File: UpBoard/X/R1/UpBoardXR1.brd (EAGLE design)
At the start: 88.9 x 76.2 mm, 79 parts, among them CN1 100nF, CN2 100nF, CN3 100nF, CN4 100nF, IC1 SAM3X8E(ARDUINO), IC2 W25N01GVZEIG/IT, Q2 MBT3904DW2T1, X1 16POS_RIBBON, X2 16POS_RIBBON, X3 16POS_RIBBON, X4 16POS_RIBBON, Y1 FH1200001, Y2 ABS05

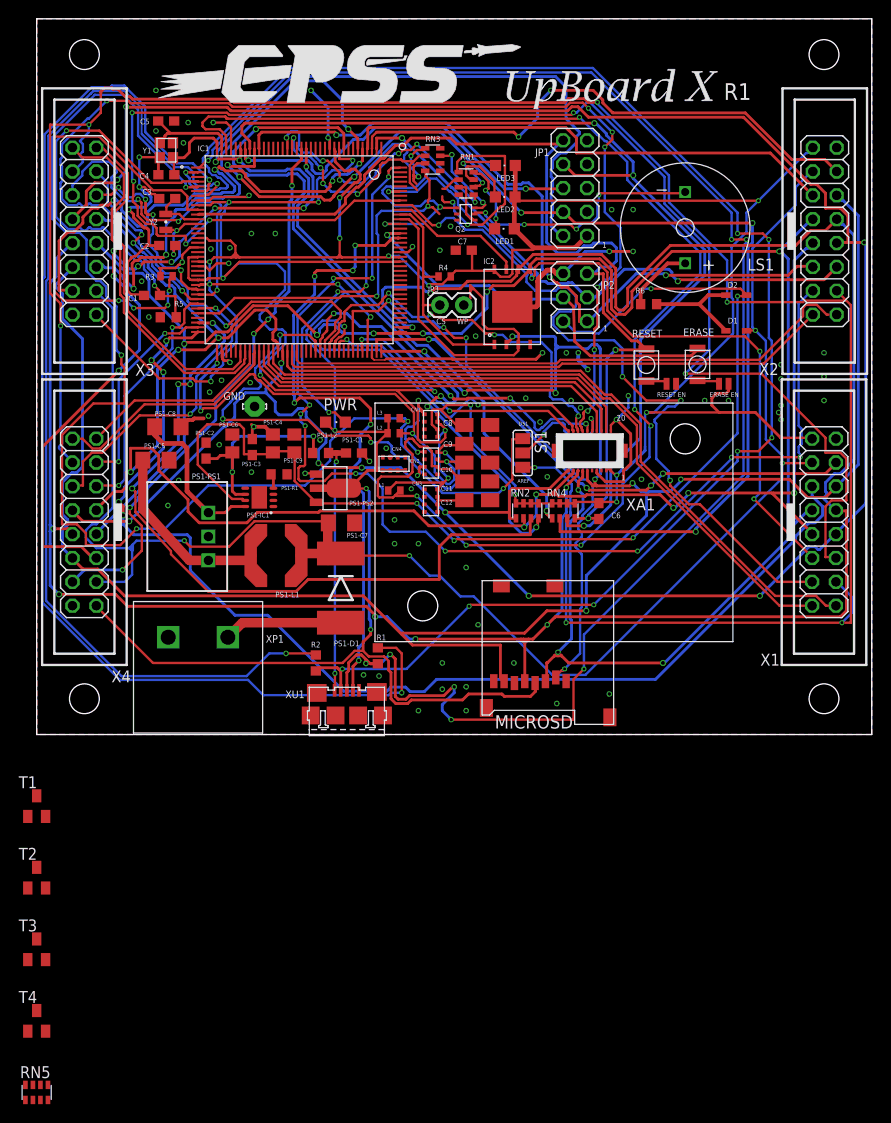
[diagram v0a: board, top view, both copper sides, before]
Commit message: Added in and routed bjt arrays
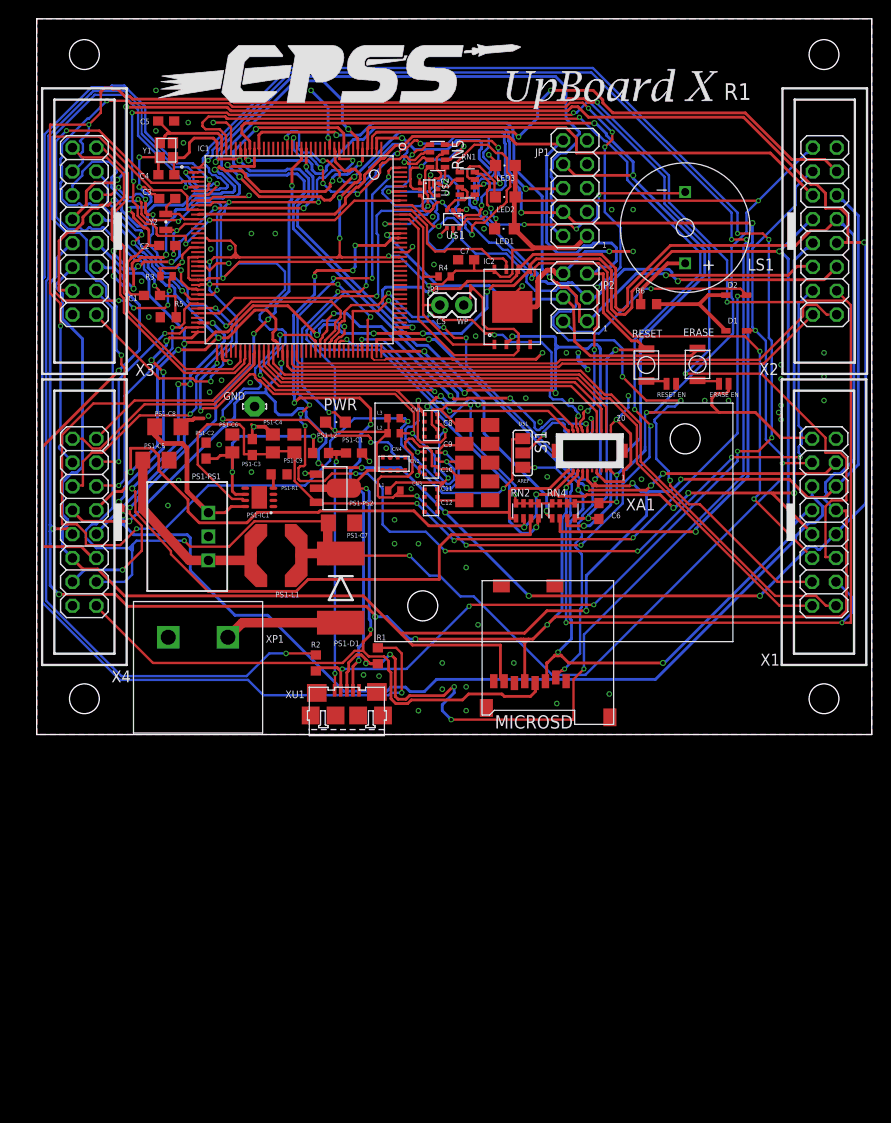
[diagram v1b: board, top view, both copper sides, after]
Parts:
- removed Q2: MBT3904DW2T1, CPSS_IC:SOT-363
- removed RN3: 100K, resistor-net:CTS742C083
- removed T1, T2, T3, T4: (no value), transistor:SOT23-BEC
- added U$1, U$2: FFB2222A, CPSS_IC:SC-88
- moved RN5 108.4 mm to (42.7, 61.6), turned to 270 degrees
- moved C7 1.05 mm to (45.7, 50.5)
- moved RN1 0.13 mm to (45.8, 58.7)
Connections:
- removed net 3.3: RN5.4
- removed net N$18: RN5.6, T3.B
- net D11: now also RN5.2; no longer RN3.2, RN5.1
- net D12: now also RN5.3; no longer RN3.3, RN5.2
- net D13: now also RN5.4; no longer RN3.4, RN5.3
- net D9: now also RN5.1; no longer Q2.P$1, RN3.1
- net GND: now also RN1.8, U$1.P$1, U$1.P$4, U$2.P$1, U$2.P$4; no longer Q2.P$6, RN3.5, RN3.6, RN3.7, RN3.8, T1.E, T2.E, T3.E, T4.E
- net N$10: now also U$1.P$3; no longer T3.C
- net N$11: now also U$2.P$6; no longer T2.C
- net N$12: now also U$2.P$3; no longer T1.C
- net N$16: now also RN5.6, U$2.P$2; no longer RN5.8, T1.B
- net N$17: now also U$2.P$5; no longer T2.B
- net N$19: now also RN5.8, U$1.P$2; no longer RN5.5, T4.B
- net N$33: now also U$1.P$6; no longer Q2.P$5
- net N$8: now also RN5.5, U$1.P$5; no longer RN1.8, T4.C
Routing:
- net N$19: track 0.00 -> 18.8 mm, vias 0 -> 2
- net N$8: track 0.00 -> 14.4 mm, vias 0 -> 2
- net N$16: track 0.00 -> 12.4 mm, vias 0 -> 2
- net N$5: track 48.9 -> 57.9 mm
- net TX/D1: track 60.7 -> 69.1 mm
- net N$12: track 21.1 -> 27.6 mm
- net N$17: track 0.00 -> 5.61 mm
- net D9: track 28.2 -> 23.1 mm, vias 3 -> 2
- net JTAG_TCK: track 120.6 -> 124.5 mm
- net D12: track 29.5 -> 25.7 mm
- net D11: track 25.2 -> 22.5 mm
- net JTAG_TDO: track 40.9 -> 43.4 mm
- net N$33: track 26.4 -> 28.8 mm
- net RX/D0: track 78.8 -> 81.0 mm
- net D3: track 79.1 -> 80.9 mm
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
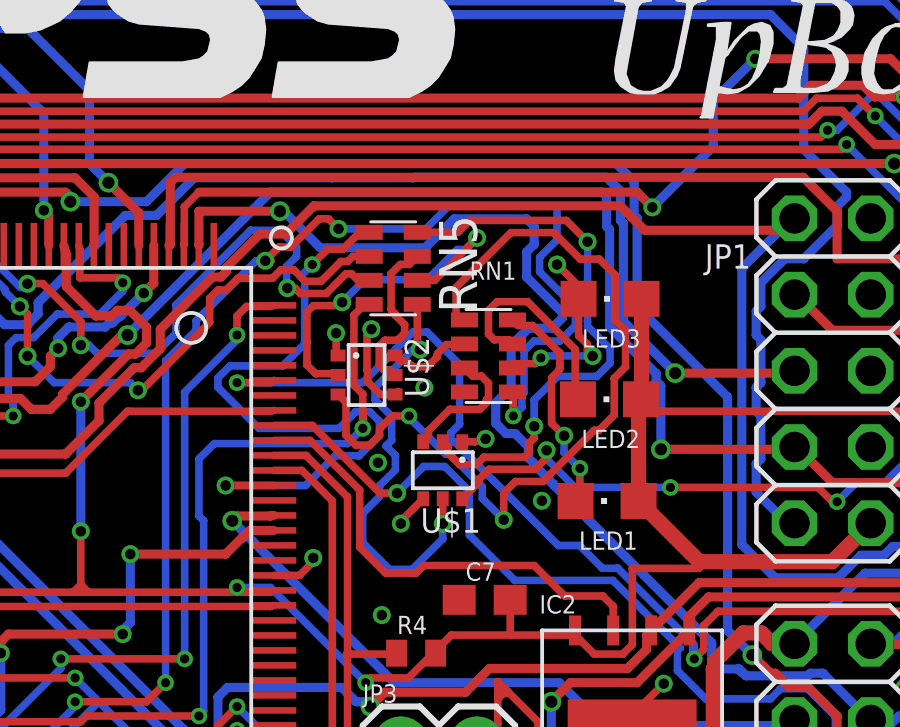
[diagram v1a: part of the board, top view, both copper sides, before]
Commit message: Fixed naming and silkscreen
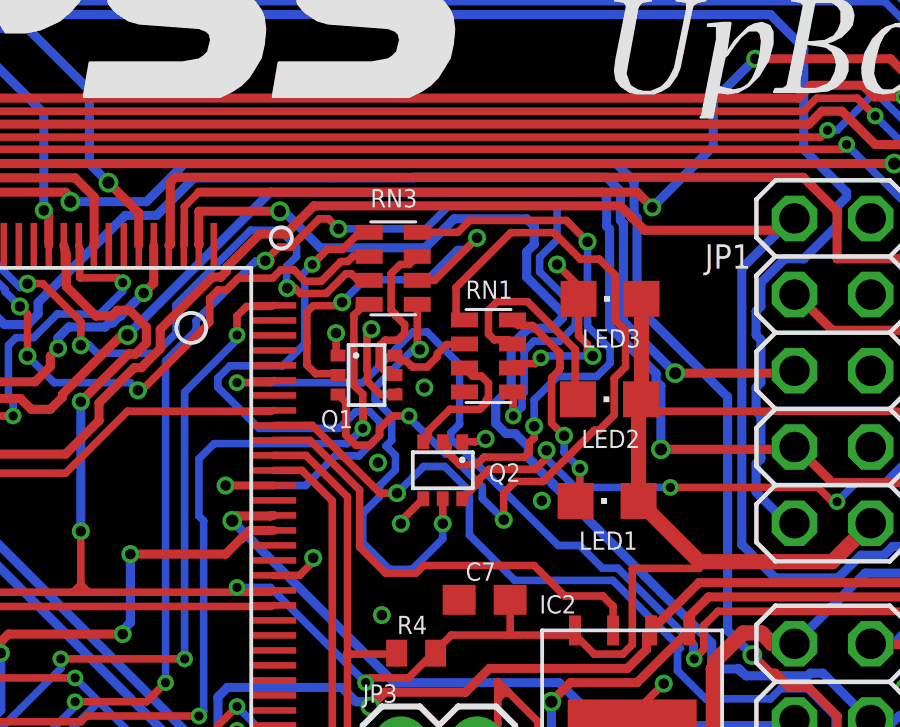
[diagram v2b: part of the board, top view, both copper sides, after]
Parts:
- renumbered RN5 to RN3, U$1 to Q2, U$2 to Q1
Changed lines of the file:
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@@
 <attribute name="MF" value="" x="45.847" y="58.674" size="1.778" layer="27" rot="R90" display="off"/>
 <attribute name="MPN" value="" x="45.847" y="58.674" size="1.778" layer="27" rot="R90" display="off"/>
-<attribute name="NAME" x="45.212" y="61.214" size="0.6096" layer="25"/>
+<attribute name="NAME" x="45.085" y="60.579" size="0.6096" layer="25"/>
 <attribute name="OC_FARNELL" value="unknown" x="45.847" y="58.674" size="1.778" layer="27" rot="R90" display="off"/>
 <attribute name="OC_NEWARK" value="unknown" x="45.847" y="58.674" size="1.778" layer="27" rot="R90" display="off"/>
@@
 <element name="SJ3" library="CPSS_CONNECTOR" package="SOLBRDG" value="SOLBRDG" x="73.152" y="37.338" smashed="yes" rot="R270"/>
 <element name="SJ2" library="CPSS_CONNECTOR" package="SOLBRDG" value="SOLBRDG" x="67.564" y="37.338" rot="R270"/>
-<element name="RN5" library="resistor-net" library_urn="urn:adsk.eagle:library:343" package="CTS742C083" package3d_urn="urn:adsk.eagle:package:24985/1" value="4.7K" x="42.672" y="61.595" rot="R270">
+<element name="RN3" library="resistor-net" library_urn="urn:adsk.eagle:library:343" package="CTS742C083" package3d_urn="urn:adsk.eagle:package:24985/1" value="4.7K" x="42.672" y="61.595" smashed="yes" rot="R270">
 <attribute name="MF" value="" x="42.672" y="61.595" size="1.778" layer="27" rot="R270" display="off"/>
 <attribute name="MPN" value="" x="42.672" y="61.595" size="1.778" layer="27" rot="R270" display="off"/>
+<attribute name="NAME" x="41.91" y="63.627" size="0.6096" layer="25"/>
 <attribute name="OC_FARNELL" value="unknown" x="42.672" y="61.595" size="1.778" layer="27" rot="R270" display="off"/>
 <attribute name="OC_NEWARK" value="unknown" x="42.672" y="61.595" size="1.778" layer="27" rot="R270" display="off"/>
 </element>
-<element name="U$1" library="CPSS_IC" package="SC-88" value="FFB2222A" x="44.323" y="54.864" rot="R180"/>
-<element name="U$2" library="CPSS_IC" package="SC-88" value="FFB2222A" x="41.783" y="58.039" rot="R270"/>
+<element name="Q2" library="CPSS_IC" package="SC-88" value="FFB2222A" x="44.323" y="54.864" smashed="yes" rot="R180">
+<attribute name="NAME" x="45.847" y="54.483" size="0.6096" layer="25"/>
+</element>
+<element name="Q1" library="CPSS_IC" package="SC-88" value="FFB2222A" x="41.783" y="58.039" smashed="yes" rot="R270">
+<attribute name="NAME" x="40.259" y="56.261" size="0.6096" layer="25"/>
+</element>
 </elements>
 <signals>
@@
 <wire x1="40.86573125" y1="56.261" x2="38.19525" y2="56.261" width="0.254" layer="16"/>
 <wire x1="38.19525" y1="56.261" x2="36.83" y2="57.62625" width="0.254" layer="16"/>
-<contactref element="RN5" pad="1"/>
+<contactref element="RN3" pad="1"/>
 <wire x1="41.55425" y1="62.795" x2="41.872" y2="62.795" width="0.254" layer="1"/>
 <wire x1="40.98925" y1="62.23" x2="41.55425" y2="62.795" width="0.254" layer="1"/>
@@
 <wire x1="11.72845" y1="53.93055" x2="11.938" y2="53.721" width="0.3048" layer="1"/>
 <wire x1="11.938" y1="53.721" x2="11.938" y2="52.06" width="0.3048" layer="1"/>
-<contactref element="U$1" pad="P$4"/>
-<contactref element="U$2" pad="P$1"/>
-<contactref element="U$2" pad="P$4"/>
+<contactref element="Q2" pad="P$4"/>
+<contactref element="Q1" pad="P$1"/>
+<contactref element="Q1" pad="P$4"/>
 <contactref element="RN1" pad="8"/>
-<contactref element="U$1" pad="P$1"/>
+<contactref element="Q2" pad="P$1"/>
 <wire x1="44.973" y1="55.814" x2="45.047" y2="55.888" width="0.254" layer="1"/>
 <via x="40.767" y="59.436" extent="1-16" drill="0.35"/>
@@
 <wire x1="36.703" y1="55.753" x2="36.195" y2="55.245" width="0.254" layer="16"/>
 <wire x1="41.656" y1="56.89286875" x2="41.656" y2="56.261" width="0.254" layer="1"/>
-<contactref element="RN5" pad="4"/>
+<contactref element="RN3" pad="4"/>
 <wire x1="41.656" y1="56.261" x2="41.656" y2="57.404" width="0.254" layer="1"/>
 <wire x1="41.656" y1="57.404" x2="41.3624" y2="57.6976" width="0.254" layer="1"/>
@@
 <via x="57.4675" y="53.81625" extent="1-16" drill="0.3048"/>
 <via x="59.84875" y="57.4675" extent="1-16" drill="0.3048"/>
-<contactref element="U$1" pad="P$6"/>
+<contactref element="Q2" pad="P$6"/>
 <wire x1="45.86625" y1="54.8965" x2="47.4035" y2="54.8965" width="0.254" layer="1"/>
 <wire x1="45.86625" y1="54.8965" x2="45.525675" y2="54.555925" width="0.254" layer="1"/>
@@
 <wire x1="27.3332" y1="63.5282" x2="27.35558125" y2="63.5282" width="0.254" layer="1"/>
 <via x="27.35558125" y="63.5282" extent="1-16" drill="0.35"/>
-<contactref element="RN5" pad="2"/>
+<contactref element="RN3" pad="2"/>
 <wire x1="41.1575875" y1="61.8236" x2="41.3289875" y2="61.995" width="0.254" layer="1"/>
 <wire x1="41.3289875" y1="61.995" x2="41.872" y2="61.995" width="0.254" layer="1"/>
@@
 <wire x1="26.59918125" y1="63.5282" x2="26.59918125" y2="63.721025" width="0.254" layer="16"/>
 <wire x1="26.59918125" y1="63.721025" x2="27.11475625" y2="64.2366" width="0.254" layer="16"/>
-<contactref element="RN5" pad="3"/>
+<contactref element="RN3" pad="3"/>
 <wire x1="41.0972" y1="61.4172" x2="41.275" y2="61.4172" width="0.254" layer="1"/>
 <wire x1="41.275" y1="61.4172" x2="41.4972" y2="61.195" width="0.254" layer="1"/>
@@
 <wire x1="36.10136875" y1="59.85036875" x2="36.10136875" y2="59.52963125" width="0.254" layer="16"/>
 <wire x1="46.6725" y1="57.0865" x2="46.6725" y2="56.67375" width="0.254" layer="16"/>
-<wire x1="44.5251375" y1="63.6778" x2="45.72" y2="63.6778" width="0.254" layer="16"/>
 <via x="40.8480125" y="62.9109875" extent="1-16" drill="0.35"/>
-<wire x1="45.72" y1="63.6778" x2="46.0258625" y2="63.6778" width="0.254" layer="16"/>
 <wire x1="40.8480125" y1="62.9109875" x2="43.758325" y2="62.9109875" width="0.254" layer="16"/>
 <wire x1="43.758325" y1="62.9109875" x2="44.5251375" y2="63.6778" width="0.254" layer="16"/>
@@
 <wire x1="40.2029125" y1="63.246" x2="40.513" y2="63.246" width="0.254" layer="1"/>
 <wire x1="40.513" y1="63.246" x2="40.8480125" y2="62.9109875" width="0.254" layer="1"/>
-<wire x1="46.0258625" y1="63.6778" x2="48.0822" y2="63.6778" width="0.254" layer="16"/>
+<wire x1="44.5251375" y1="63.6778" x2="48.0822" y2="63.6778" width="0.254" layer="16"/>
 <wire x1="48.0822" y1="63.6778" x2="48.133" y2="63.627" width="0.254" layer="16"/>
 <wire x1="48.133" y1="63.627" x2="48.133" y2="62.544225" width="0.254" layer="16"/>
 <wire x1="47.5516" y1="61.962825" x2="47.5516" y2="61.481175" width="0.254" layer="16"/>
 <wire x1="48.7426" y1="60.290175" x2="48.7426" y2="59.69" width="0.254" layer="16"/>
-<wire x1="47.5516" y1="61.481175" x2="48.1663875" y2="60.8663875" width="0.254" layer="16"/>
-<wire x1="48.1663875" y1="60.8663875" x2="48.7426" y2="60.290175" width="0.254" layer="16"/>
+<wire x1="47.5516" y1="61.481175" x2="48.7426" y2="60.290175" width="0.254" layer="16"/>
 <wire x1="48.133" y1="62.544225" x2="47.5516" y2="61.962825" width="0.254" layer="16"/>
 <wire x1="47.36178125" y1="59.1693" x2="47.03445" y2="58.84196875" width="0.254" layer="16"/>
@@
 <signal name="N$10">
 <contactref element="RN1" pad="7"/>
-<contactref element="U$1" pad="P$3"/>
+<contactref element="Q2" pad="P$3"/>
 <wire x1="44.939" y1="58.166" x2="45.047" y2="58.274" width="0.254" layer="1"/>
 <wire x1="43.8436" y1="55.9846" x2="43.673" y2="55.814" width="0.254" layer="1"/>
@@
 <wire x1="44.45" y1="59.055" x2="44.7675" y2="59.055" width="0.254" layer="1"/>
 <wire x1="44.7675" y1="59.055" x2="45.047" y2="59.074" width="0.254" layer="1"/>
-<contactref element="U$2" pad="P$6"/>
+<contactref element="Q1" pad="P$6"/>
 <wire x1="42.733" y1="58.689" x2="42.9036" y2="58.5184" width="0.254" layer="1"/>
 <wire x1="42.9036" y1="58.5184" x2="43.09873125" y2="58.5184" width="0.254" layer="1"/>
@@
 <wire x1="44.7675" y1="60.0075" x2="45.047" y2="59.874" width="0.254" layer="1"/>
 <via x="43.19905" y="56.67375" extent="1-16" drill="0.3048"/>
-<contactref element="U$2" pad="P$3"/>
+<contactref element="Q1" pad="P$3"/>
 <wire x1="41.0972" y1="56.02953125" x2="41.42453125" y2="55.7022" width="0.254" layer="1"/>
 <wire x1="41.42453125" y1="55.7022" x2="41.88746875" y2="55.7022" width="0.254" layer="1"/>
@@
 </signal>
 <signal name="N$16">
-<contactref element="U$2" pad="P$2"/>
-<contactref element="RN5" pad="6"/>
+<contactref element="Q1" pad="P$2"/>
+<contactref element="RN3" pad="6"/>
 <wire x1="40.7894" y1="58.0826" x2="40.833" y2="58.039" width="0.254" layer="1"/>
 <wire x1="40.7894" y1="58.0826" x2="40.08626875" y2="58.0826" width="0.254" layer="1"/>
@@
 </signal>
 <signal name="N$17">
-<contactref element="U$2" pad="P$5"/>
-<contactref element="RN5" pad="7"/>
+<contactref element="Q1" pad="P$5"/>
+<contactref element="RN3" pad="7"/>
 <wire x1="43.472" y1="61.995" x2="43.2014" y2="61.7244" width="0.254" layer="1"/>
 <wire x1="43.2014" y1="61.7244" x2="42.90626875" y2="61.7244" width="0.254" layer="1"/>
@@
 </signal>
 <signal name="N$19">
-<contactref element="U$1" pad="P$2"/>
-<contactref element="RN5" pad="8"/>
+<contactref element="Q2" pad="P$2"/>
+<contactref element="RN3" pad="8"/>
 <wire x1="43.472" y1="62.795" x2="44.827775" y2="62.795" width="0.254" layer="1"/>
 <wire x1="44.827775" y1="62.795" x2="45.225175" y2="63.1924" width="0.254" layer="1"/>
@@
 </signal>
 <signal name="N$8">
-<contactref element="RN5" pad="5"/>
-<contactref element="U$1" pad="P$5"/>
+<contactref element="RN3" pad="5"/>
+<contactref element="Q2" pad="P$5"/>
 <wire x1="43.472" y1="60.395" x2="43.472" y2="58.9784" width="0.254" layer="1"/>
 <wire x1="43.472" y1="58.9784" x2="43.561" y2="58.8894" width="0.254" layer="1"/>
